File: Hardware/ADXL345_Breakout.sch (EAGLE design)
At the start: 11 parts, among them U2 ADXL345PATRICK

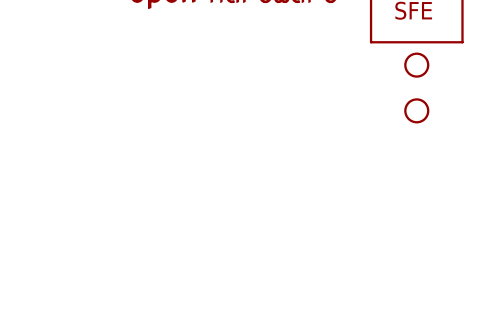
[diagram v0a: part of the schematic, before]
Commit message: Updating README, versions on board files
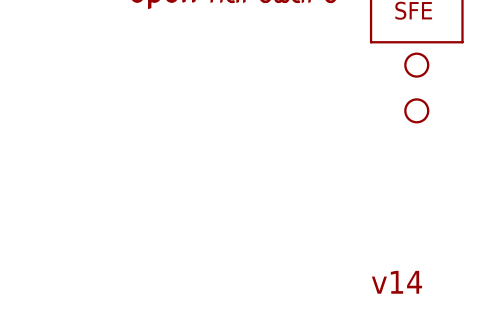
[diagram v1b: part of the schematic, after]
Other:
- note added: "v14"
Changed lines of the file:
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@@
 <?xml version="1.0" encoding="utf-8"?>
 <!DOCTYPE eagle SYSTEM "eagle.dtd">
-<eagle version="6.4">
+<eagle version="6.5.0">
 <drawing>
 <settings>
@@
 <text x="166.37" y="11.684" size="2.54" layer="94" font="vector">Jim Lindblom</text>
 <text x="149.098" y="6.604" size="2.54" layer="94" font="vector">Revised by: Patrick Alberts</text>
+<text x="238.76" y="7.62" size="2.54" layer="94">v14</text>
 </plain>
 <instances>
